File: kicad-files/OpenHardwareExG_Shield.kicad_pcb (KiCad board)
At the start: 4 copper layers, 191 parts, among them P1 CONN_1, P10 CONN_10X2, P11 CONN_1, P12 CONN_1, P13 CONN_1, P14 CONN_1, P15 CONN_1, P16 CONN_1, P17 CONN_1, P18 CONN_1, P19 ARDUINO_SHIELD, P2 CONN_1, P20 CONN_3X2, P21 CONN_3X2, P22 CONN_4, P23 CONN_1, P24 CONN_1, P25 CONN_1, P26 CONN_1, P27 CONN_1, P28 CONN_1, P29 CONN_1, P3 CONN_1, P30 CONN_1, P31 CONN_1, P32 CONN_1, P33 CONN_1, P34 CONN_1, P35 CONN_1, P36 CONN_1, P37 CONN_1, P38 CONN_1, P39 CONN_1, P4 CONN_1, P40 CONN_1, P41 CONN_1, P42 CONN_1, P43 CONN_1, P44 CONN_1, P45 CONN_1, P46 CONN_1, P47 CONN_1, P48 CONN_1, P49 CONN_1, P5 CONN_1, P50 CONN_1, P51 CONN_1, P52 CONN_1, P53 CONN_1, P54 CONN_1, P55 CONN_1, P56 CONN_3, P6 CONN_1, P7 CONN_1, P8 CONN_1, P9 CONN_1, U1 ADS1299, U2 BT1308W-600D, U3 TL431BIDBZR, U4 873-AAT3220IGY-33T1, U5 ADUM6000, U6 SI8663, U7 74LS02, U8 74LS00, U9 74LS125

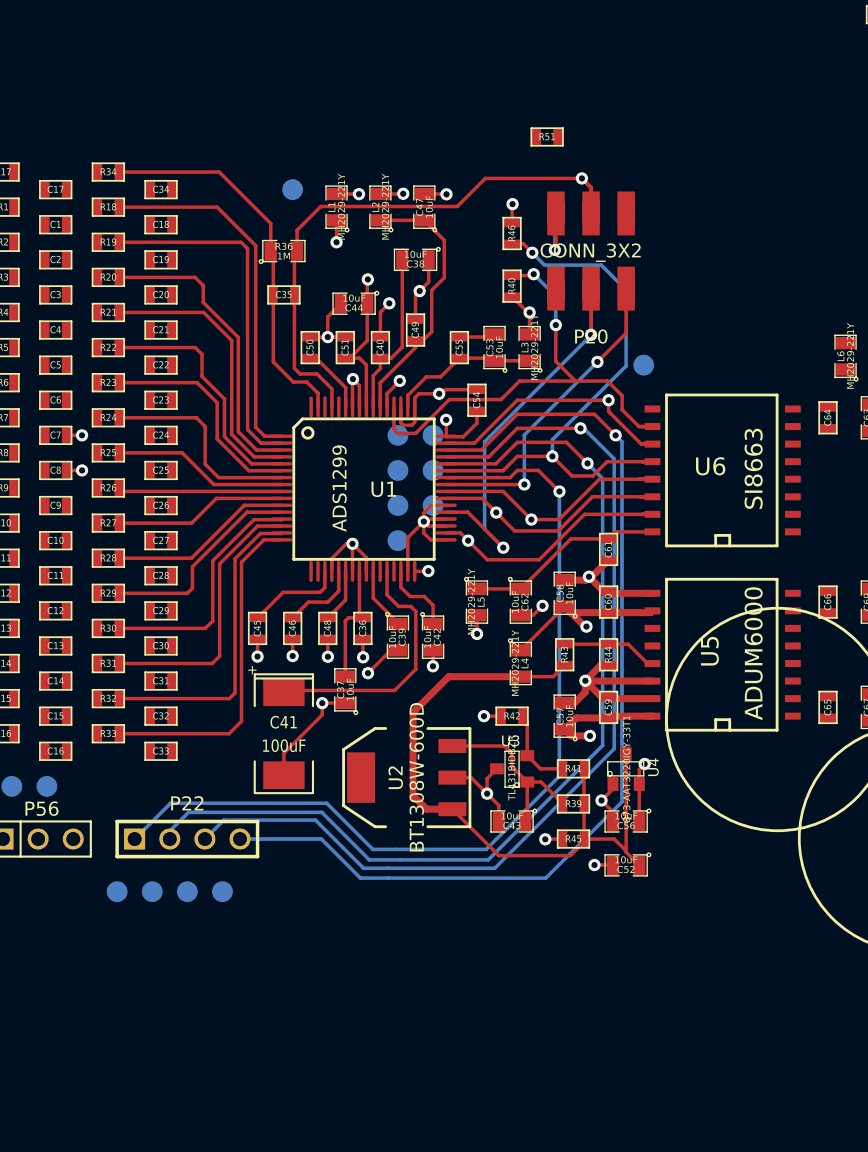
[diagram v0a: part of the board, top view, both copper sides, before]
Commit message: move GPIO north, begin to cinch-in south end footprints
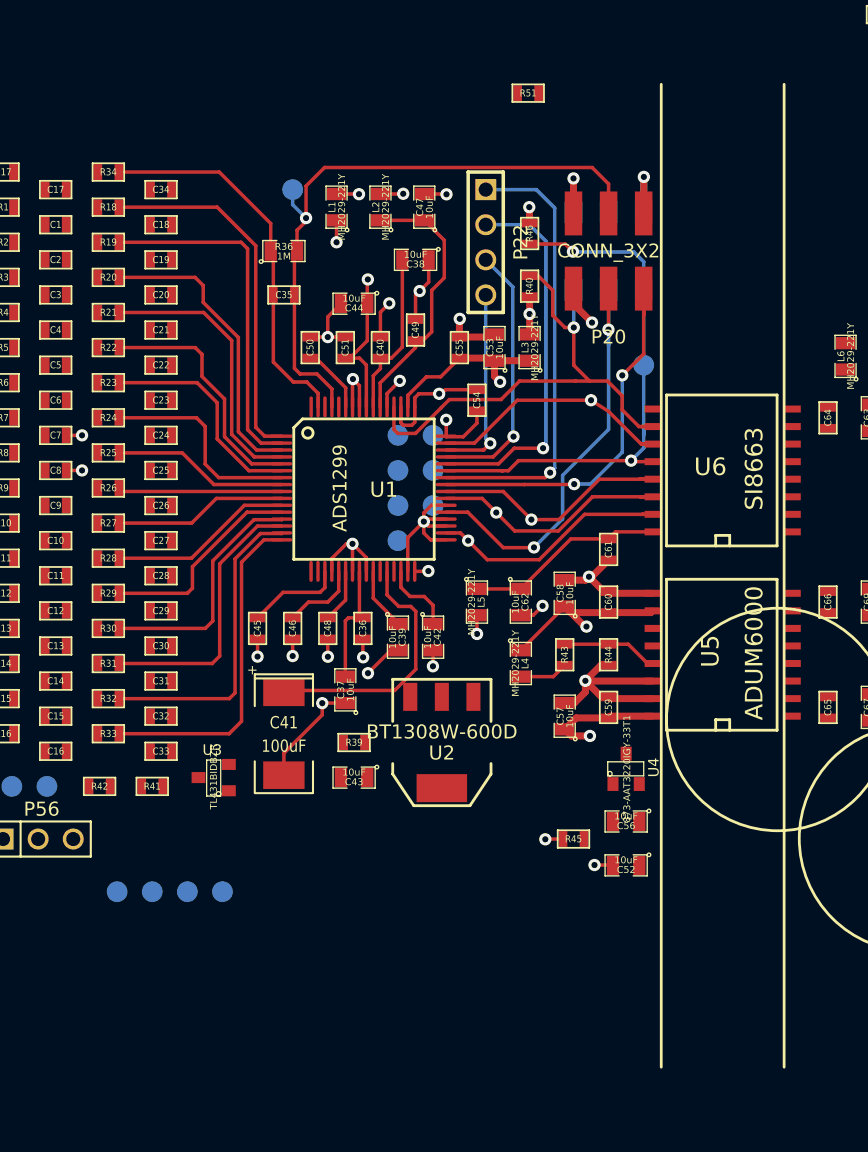
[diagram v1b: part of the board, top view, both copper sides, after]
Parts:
- moved P22 48.3 mm to (102.9, 41.9), turned to 270 degrees
- moved R41 30.5 mm to (78.7, 81.3)
- moved R42 30.3 mm to (74.9, 81.3)
- moved U3 21.6 mm to (83.2, 80.6)
- moved R39 16.5 mm to (93.3, 78.1)
- moved C43 11.9 mm to (93.3, 80.6)
- moved U2 3.59 mm to (99.7, 78.1), turned to 180 degrees
- moved R51 3.46 mm to (105.9, 31.1)
- moved P20 1.27 mm to (111.8, 42.5)
- moved P21 1.27 mm to (111.8, 42.5)
- moved R40 1.27 mm to (106.0, 45.1)
- moved R46 1.27 mm to (106.0, 41.3)
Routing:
- net /ADS129x_GPIO4_ISO: track 71.8 -> 14.3 mm
- net /ADS129x_GPIO3_ISO: track 70.1 -> 19.1 mm
- net /VIN_ISO: track 53.5 -> 6.80 mm
- net /ADS129x_GPIO2_ISO: track 69.7 -> 27.4 mm
- net /ADS129x_GPIO1_ISO: track 65.0 -> 32.5 mm
- net N-0000035: track 13.2 -> 0.00 mm
- net AGND: track 57.5 -> 48.7 mm, vias 19 -> 17
- net N-0000034: track 5.98 -> 0.00 mm
- net DGND: track 60.2 -> 65.8 mm, vias 8 -> 10
- net /ADS129x_DAISY_IN_ISO: track 22.9 -> 28.1 mm
- net /3.3V_ISO: track 10.3 -> 5.38 mm, vias 4 -> 3
- net /BIASINV: track 43.3 -> 45.7 mm
- net /MASTER_ISO: track 35.0 -> 37.0 mm, vias 2 -> 1
- net +3.3VADC: track 17.0 -> 18.4 mm, vias 2 -> 3
- net /ADS129x_DOUT_ISO: track 40.4 -> 39.4 mm
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
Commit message: lay tracks for south end
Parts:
- moved P29 37.6 mm to (28.6, 83.8)
- moved P30 37.6 mm to (31.1, 83.8)
- moved P31 37.6 mm to (33.7, 83.8)
- moved R45 15.1 mm to (102.2, 71.8)
- moved C52 12.7 mm to (105.4, 76.8), turned to 90 degrees
- moved P56 6.75 mm to (65.4, 80.6)
- moved U4 6.48 mm to (106.7, 81.3), turned to 90 degrees
- moved C56 3.59 mm to (110.5, 81.3), turned to 270 degrees
- turned C43 to 0 degrees
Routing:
- net /VIN_ISO: track 6.80 -> 33.3 mm, vias 2 -> 3
- net N-0000035: track 0.00 -> 18.0 mm
- net N-0000034: track 0.00 -> 11.5 mm
- net DGND: track 65.8 -> 72.3 mm
- net /3.3V_ISO: track 5.38 -> 8.15 mm
- net AGND: track 48.7 -> 50.2 mm, vias 17 -> 20

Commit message: place GPIO PINS and digital test-points
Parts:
- removed P56: CONN_3, PIN_ARRAY_3X1
- P22: value CONN_4 -> CONN_7; footprint PIN_ARRAY_4x1 -> PIN_ARRAY_7x1
- moved P30 76.3 mm to (94.0, 40.6)
- moved P31 76.3 mm to (96.5, 40.6)
- moved P29 74.2 mm to (88.9, 40.6)
- moved P32 59.2 mm to (106.7, 38.1)
- moved P33 55.8 mm to (106.7, 40.6)
- moved P35 50.6 mm to (99.1, 40.6)
- moved P34 38.1 mm to (104.1, 58.4)
- moved P36 15.2 mm to (111.8, 61.0)
- moved P26 13.7 mm to (109.2, 50.8)
- moved P38 13.7 mm to (109.2, 63.5)
- moved R46 10.6 mm to (111.8, 50.2), turned to 0 degrees
- moved P28 10.5 mm to (109.2, 53.3)
- moved P24 8.03 mm to (106.7, 61.0)
- moved P37 7.72 mm to (83.0, 33.1)
- moved L2 7.67 mm to (102.2, 42.5), turned to 0 degrees
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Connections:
- P31 pad 1: DGND -> /DGND_ISO
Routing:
- net /ADS129x_GPIO4_ISO: track 14.3 -> 28.3 mm
- net /ADS129x_GPIO3_ISO: track 19.1 -> 27.7 mm
- net /ADS129x_DOUT_ISO: track 39.4 -> 34.0 mm
- net /AVDD1: track 19.7 -> 15.0 mm
- net /VIN_ISO: track 33.3 -> 37.3 mm, vias 3 -> 2
- net /ADS129x_DAISY_IN_ISO: track 28.1 -> 31.3 mm
- net /ADS129x_CLK_ISO: track 31.4 -> 34.4 mm
- net /ADS129x_GPIO2_ISO: track 27.4 -> 30.1 mm
- net /MASTER_ISO: track 37.0 -> 39.8 mm
- net /ADS129x_MOSI_ISO: track 17.2 -> 19.7 mm
- net /ADS129x_~CS~_ISO: track 17.2 -> 19.4 mm
- net /ADS129x_GPIO1_ISO: track 32.5 -> 30.9 mm
- net /AVDD: track 34.2 -> 35.6 mm, vias 2 -> 1
- net /ADS129x_~DRDY~_ISO: track 17.5 -> 18.7 mm
- net /BIASINV: track 45.7 -> 47.0 mm, vias 1 -> 0
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
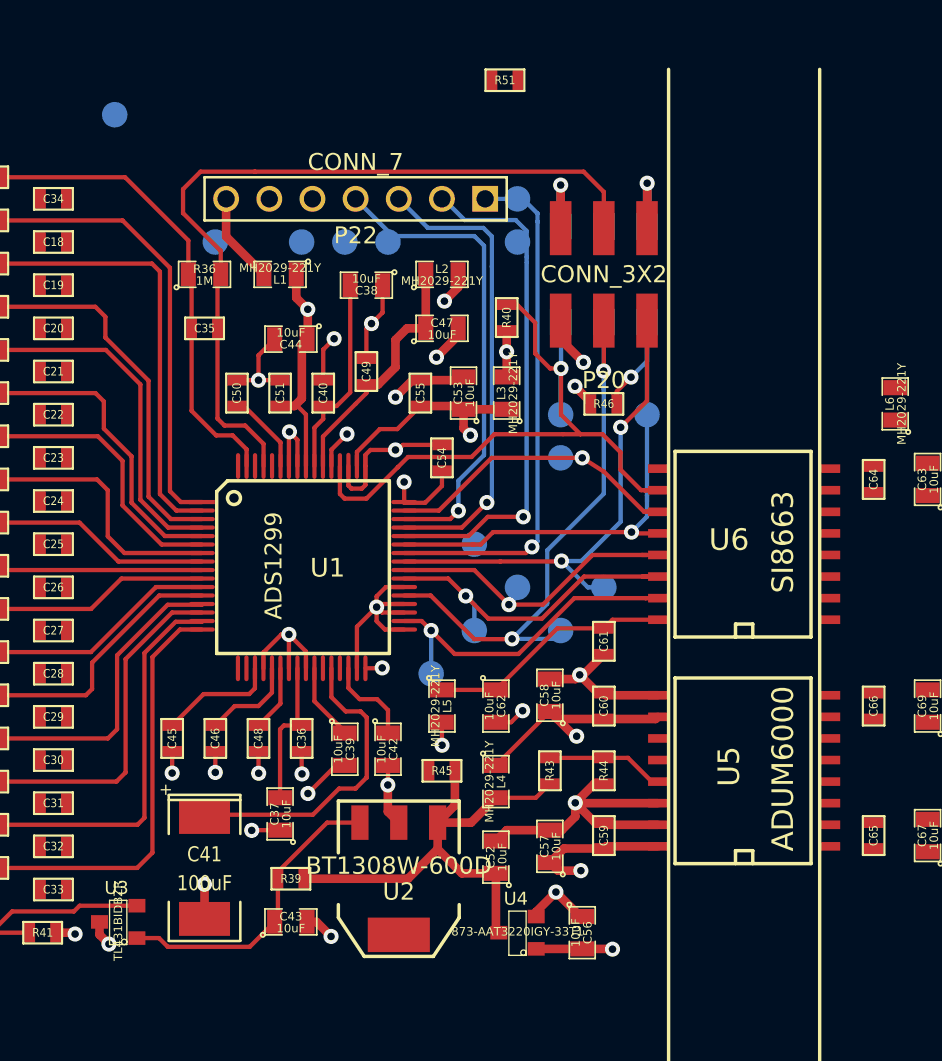
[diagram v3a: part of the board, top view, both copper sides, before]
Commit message: move regulator north of power isolator
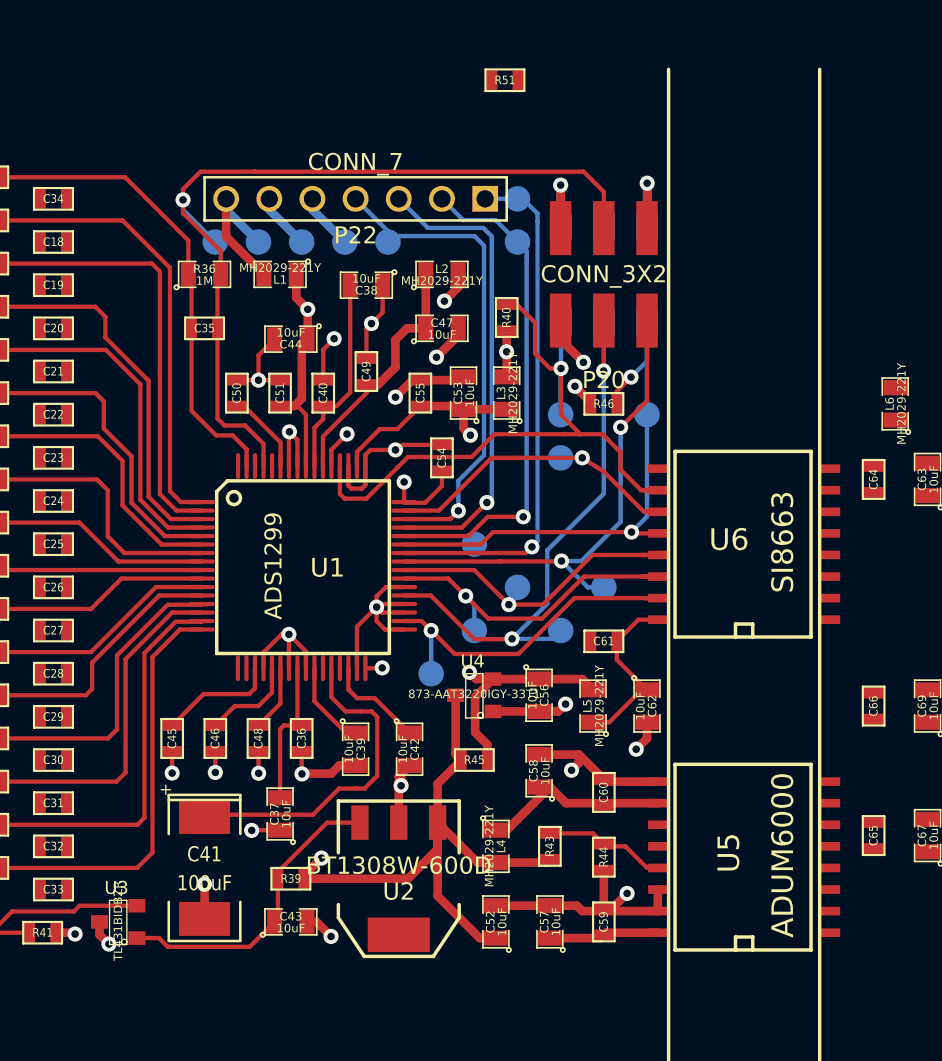
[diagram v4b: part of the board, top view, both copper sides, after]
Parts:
- moved U4 14.2 mm to (104.1, 67.3)
- moved C56 14.2 mm to (108.0, 67.3)
- moved P37 9.55 mm to (88.9, 40.6)
- moved C62 8.89 mm to (114.3, 67.9)
- moved L5 8.89 mm to (111.1, 67.9), turned to 90 degrees
- moved C60 5.08 mm to (111.8, 73.0)
- moved C59 5.08 mm to (111.8, 80.6)
- moved R44 5.08 mm to (111.8, 76.8)
- moved U5 5.08 mm to (120.0, 76.8)
- moved C58 4.49 mm to (108.0, 71.8)
- moved R43 4.45 mm to (108.6, 76.2)
- moved C57 4.44 mm to (108.6, 80.6)
- moved C52 3.81 mm to (105.4, 80.6)
- moved L4 3.81 mm to (105.4, 76.2)
- moved P29 2.54 mm to (91.4, 40.6)
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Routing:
- net /3.3V_ISO: track 8.15 -> 19.3 mm, vias 3 -> 2
- net /VIN_ISO: track 37.3 -> 48.3 mm, vias 2 -> 3
- net N-0000081: track 22.0 -> 18.1 mm, vias 2 -> 0
- net N-0000089: track 14.4 -> 10.5 mm
- net DGND: track 72.9 -> 69.2 mm
- net /DGND_ISO: track 0.00 -> 3.33 mm
- net /BIASINV: track 47.0 -> 50.2 mm, vias 0 -> 1
- net AGND: track 50.9 -> 52.8 mm, vias 20 -> 19
- net N-0000071: track 18.3 -> 19.5 mm
- net /ADS129x_GPIO2_ISO: track 30.1 -> 29.5 mm
- net N-0000070: track 4.55 -> 5.14 mm
- net N-0000092: track 5.38 -> 5.91 mm

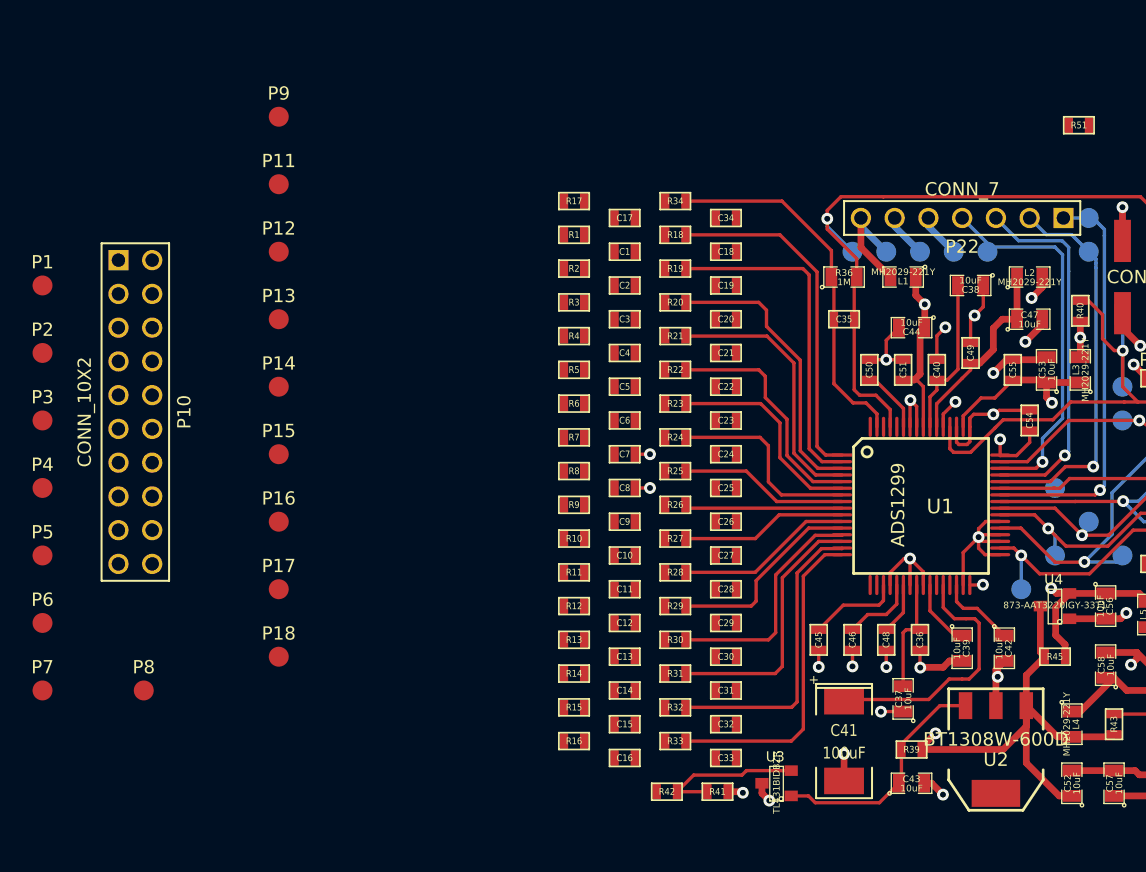
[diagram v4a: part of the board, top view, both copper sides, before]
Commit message: place EEG header and testpoints
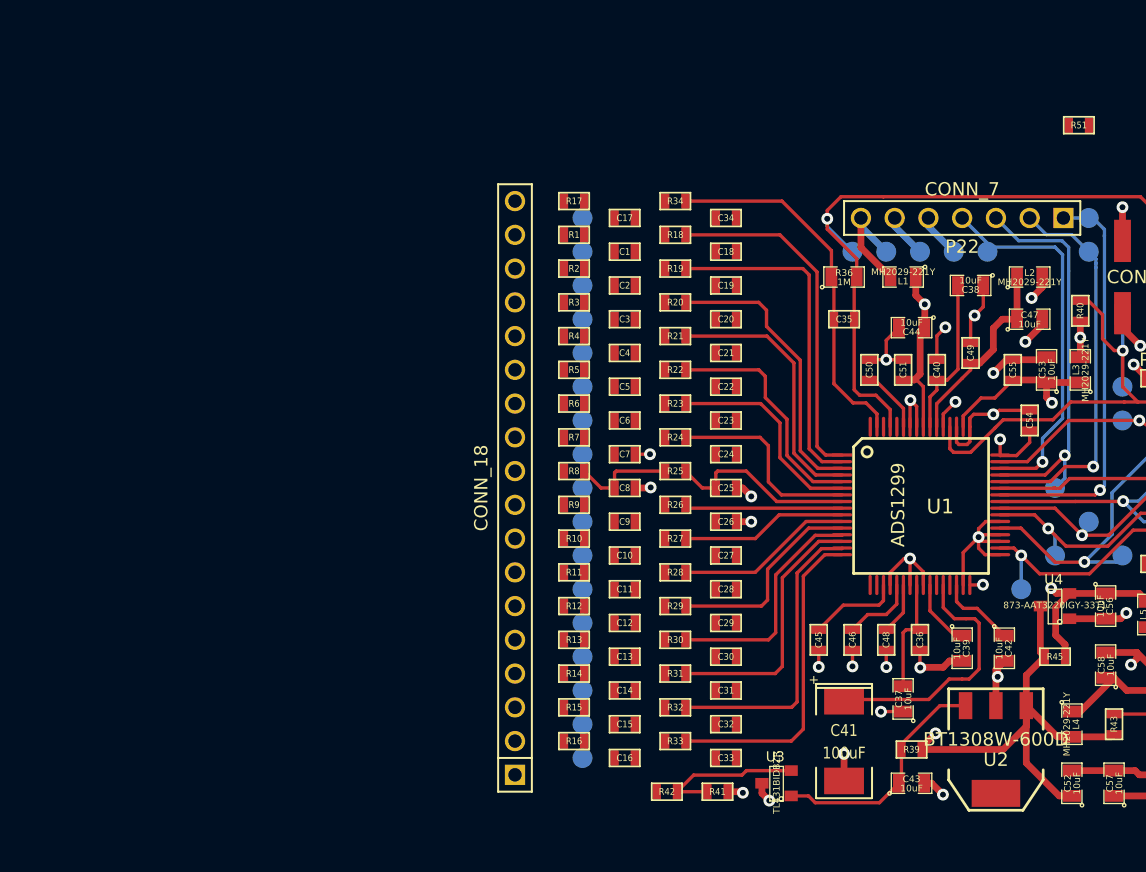
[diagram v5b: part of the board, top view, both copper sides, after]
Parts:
- P1, P11, P12, P13, P14, P15, P16, P17, P18, P2, P3, P4, P5, P6, P7, P8, P9: moved to B.Cu
- P10: value CONN_10X2 -> CONN_18; footprint pin_array_10x2 -> PIN_ARRAY_18x1
- moved P1 40.7 mm to (68.6, 40.6)
- moved P2 40.7 mm to (68.6, 45.7)
- moved P3 40.7 mm to (68.6, 50.8)
- moved P4 40.7 mm to (68.6, 55.9)
- moved P5 40.7 mm to (68.6, 61.0)
- moved P6 40.7 mm to (68.6, 66.0)
- moved P7 40.7 mm to (68.6, 71.1)
- moved P8 33.1 mm to (68.6, 76.2)
- moved P10 29.1 mm to (63.5, 58.4), turned to 90 degrees
- moved P13 24.1 mm to (68.6, 53.3)
- moved P14 24.1 mm to (68.6, 58.4)
- moved P9 24.1 mm to (68.6, 38.1)
- moved P11 24.1 mm to (68.6, 43.2)
- moved P12 24.1 mm to (68.6, 48.3)
- moved P15 24.1 mm to (68.6, 63.5)
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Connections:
- P10 pad 11: /IN4N -> /IN5N
- P10 pad 12: /IN4P -> /IN6P
- P10 pad 13: /IN3N -> /IN6N
- P10 pad 14: /IN3P -> /IN7P
- P10 pad 15: /IN2N -> /IN7N
- P10 pad 16: /IN2P -> /IN8P
- P10 pad 17: /IN1N -> /IN8N
- P10 pad 18: /IN1P -> /BIASOUT_FILT
- P10 pad 2: /BIASOUT_FILT -> /IN1P
- P10 pad 3: /IN8N -> /IN1N
- P10 pad 4: /IN8P -> /IN2P
- P10 pad 5: /IN7N -> /IN2N
- P10 pad 6: /IN7P -> /IN3P
- P10 pad 7: /IN6N -> /IN3N
- P10 pad 8: /IN6P -> /IN4P
- P10 pad 9: /IN5N -> /IN4N
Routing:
- net N-000005: track 0.00 -> 7.82 mm
- net /ADS129x_GPIO3_ISO: track 27.7 -> 30.5 mm
- net AGND: track 52.8 -> 55.4 mm, vias 19 -> 21
- net N-000004: track 12.7 -> 14.5 mm
